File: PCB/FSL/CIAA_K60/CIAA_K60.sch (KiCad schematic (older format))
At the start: 12 parts

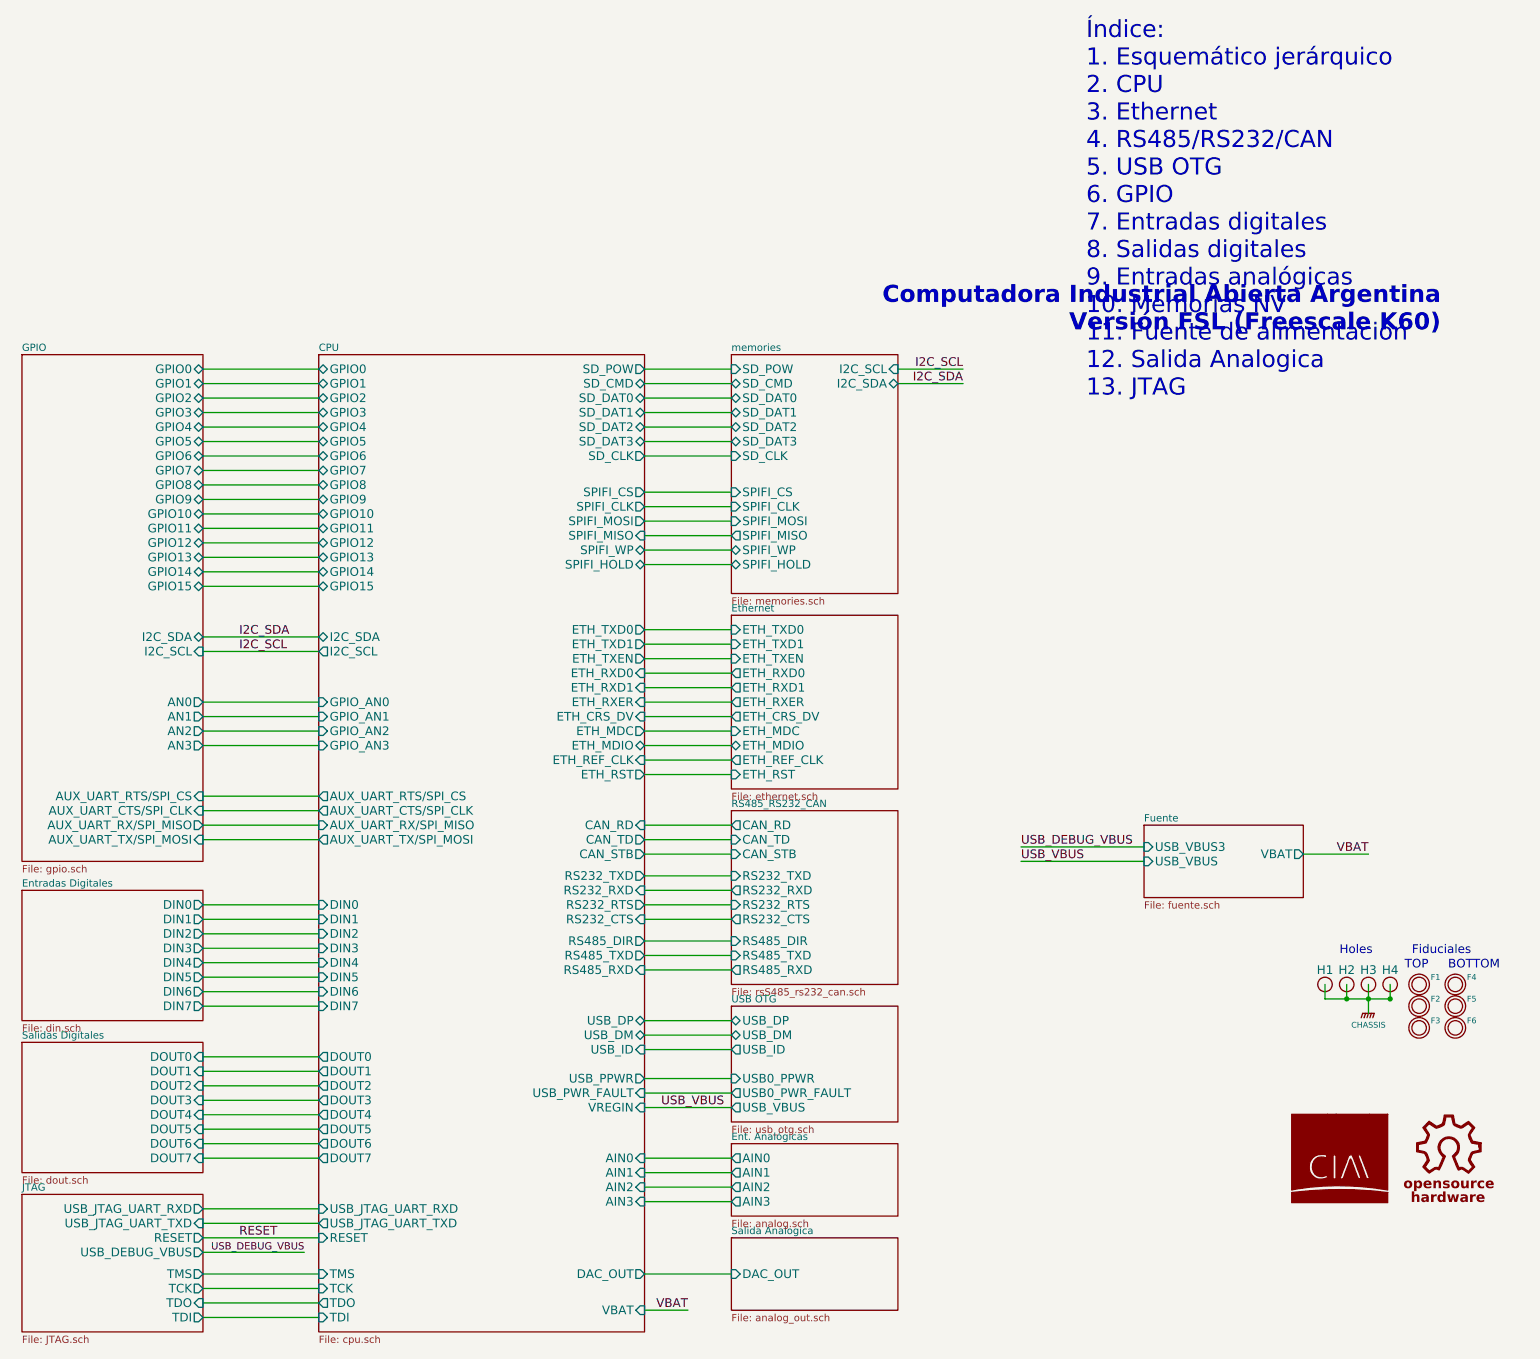
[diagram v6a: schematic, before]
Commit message: Sch files adapted to new eeschema. Fixing some text locations.
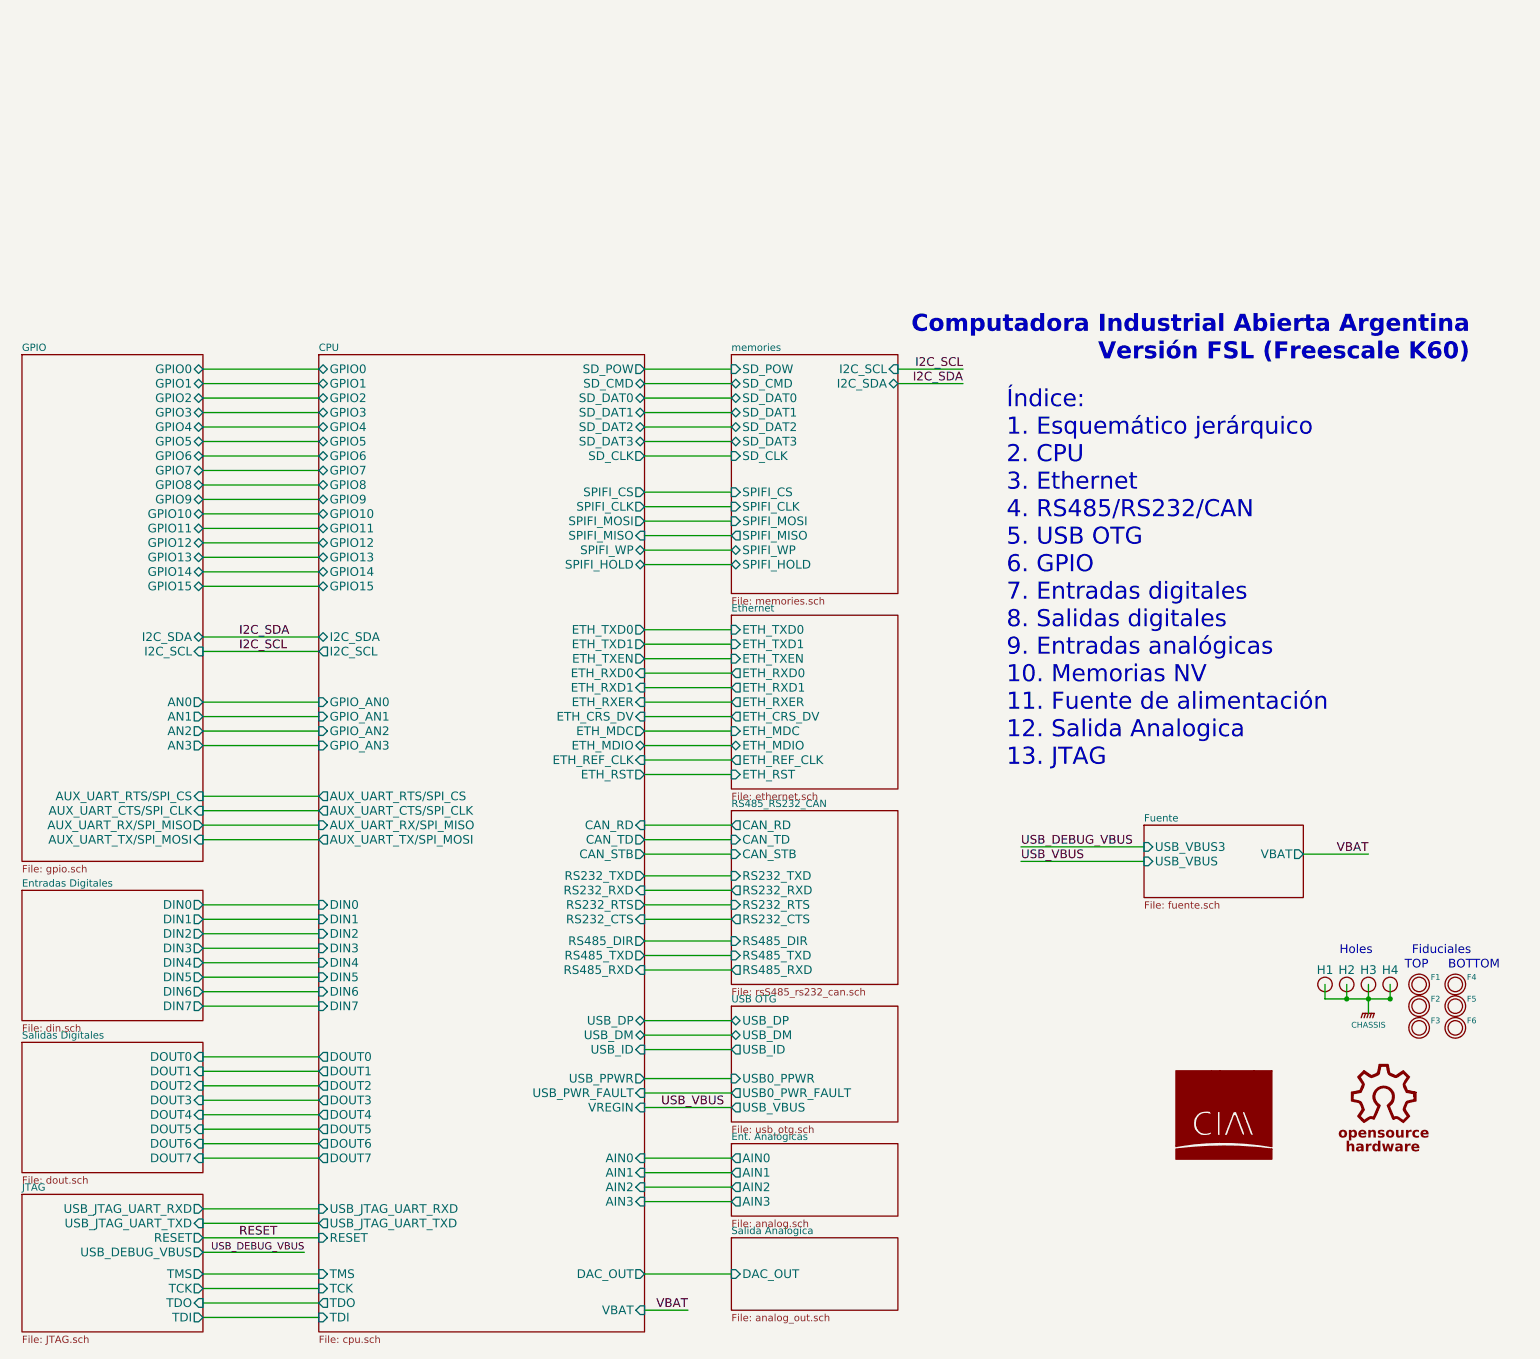
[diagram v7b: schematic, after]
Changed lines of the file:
@@
 EESchema Schematic File Version 2
 LIBS:CIAAK60LIB
-EELAYER 27 0
+LIBS:CIAA_K60-cache
+EELAYER 25 0
 EELAYER END
 $Descr A4 11693 8268
@@
 F9 "RESET" O R 2150 6950 60
 $EndSheet
-Text Notes 8250 1150 0    118  ~ 0
+Text Notes 7700 3700 0    118  ~ 0
 Índice:\n1. Esquemático jerárquico\n2. CPU\n3. Ethernet\n4. RS485/RS232/CAN\n5. USB OTG\n6. GPIO\n7. Entradas digitales\n8. Salidas digitales\n9. Entradas analógicas\n10. Memorias NV\n11. Fuente de alimentación\n12. Salida Analogica\n13. JTAG\n
-Text Notes 10700 700  2    118  ~ 24
+Text Notes 10900 900  2    118  ~ 24
 Computadora Industrial Abierta Argentina\nVersión FSL (Freescale K60)
 Text Label 7800 4250 0    60   ~ 0
@@
 L OSHWA G101
 U 1 1 53A0DEBC
-P 10750 6400
-F 0 "G101" H 10720 6800 60  0001 C CNN
-F 1 "OSHWA" H 10750 6703 60  0001 C CNN
-F 2 "OSHWA" H 10750 6400 60  0001 C CNN
-F 3 "~" H 10750 6400 60  0000 C CNN
-F 4 "LOGO DE OPEN SOURCE HARDWARE" H 10750 6400 60  0001 C CNN "Descripcion"
-	1    10750 6400
+P 10300 6050
+F 0 "G101" H 10270 6450 60  0001 C CNN
+F 1 "OSHWA" H 10300 6353 60  0001 C CNN
+F 2 "OSHWA" H 10300 6050 60  0001 C CNN
+F 3 "~" H 10300 6050 60  0000 C CNN
+F 4 "LOGO DE OPEN SOURCE HARDWARE" H 10300 6050 60  0001 C CNN "Descripcion"
+	1    10300 6050
 	1    0    0    -1
 $EndComp
@@
 L LOGO_CIAA G102
 U 1 1 53E44CA2
-P 10000 6400
-F 0 "G102" H 10000 5827 60  0001 C CNN
-F 1 "LOGO_CIAA" H 10000 6973 60  0001 C CNN
-F 2 "LOGO-CIAA" H 10000 6400 60  0001 C CNN
-F 3 "~" H 10000 6400 60  0000 C CNN
-F 4 "LOGO CIAA" H 10000 6400 60  0001 C CNN "Descripcion"
-	1    10000 6400
-	1    0    0    -1
-$EndComp
+P 9200 6100
+F 0 "G102" H 9200 5527 60  0001 C CNN
+F 1 "LOGO_CIAA" H 9200 6673 60  0001 C CNN
+F 2 "LOGO-CIAA" H 9200 6100 60  0001 C CNN
+F 3 "~" H 9200 6100 60  0000 C CNN
+F 4 "LOGO CIAA" H 9200 6100 60  0001 C CNN "Descripcion"
+	1    9200 6100
+	1    0    0    -1
+$EndComp

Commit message: Renaming symbol field-names in .sch files for KiCost integration.
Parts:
- F1, F2, F3, F4, F5, F6: Desc (none) -> FIDUCIAL; Descripcion FIDUCIAL -> (none)
- G101: Desc (none) -> LOGO DE OPEN SOURCE HARDWARE; Descripcion LOGO DE OPEN SOURCE HARDWARE -> (none)
- G102: Desc (none) -> LOGO CIAA; Descripcion LOGO CIAA -> (none)
- H1, H2, H3, H4: Desc (none) -> PCB HOLE; Descripcion PCB HOLE -> (none)
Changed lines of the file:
@@
 F 2 "Fiducial_1mm" H 10550 5250 60  0001 C CNN
 F 3 "~" H 10550 5250 60  0001 C CNN
-F 4 "FIDUCIAL" H 10600 5000 60  0001 C CNN "Descripcion"
-F 5 "~" H 10830 5400 60  0001 C CNN "Fabricante"
-F 6 "~" H 10930 5500 60  0001 C CNN "Nro. parte"
+F 4 "FIDUCIAL" H 10600 5000 60  0001 C CNN "Desc"
+F 5 "~" H 10830 5400 60  0001 C CNN "Manf"
+F 6 "~" H 10930 5500 60  0001 C CNN "Manf#"
 F 7 "~" H 11030 5600 60  0001 C CNN "Path datasheet"
-F 8 "~" H 11130 5700 60  0001 C CNN "Digikey/Mouser"
+F 8 "~" H 11130 5700 60  0001 C CNN "Digikey#"
 F 9 "~" H 11230 5800 60  0001 C CNN "Footprint estandar"
 	1    10550 5200
@@
 F 2 "PCB_HOLE" H 9750 5250 60  0001 C CNN
 F 3 "~" H 9850 5350 60  0001 C CNN
-F 4 "PCB HOLE" H 9950 5450 60  0001 C CNN "Descripcion"
-F 5 "~" H 10050 5550 60  0001 C CNN "Fabricante"
-F 6 "~" H 10150 5650 60  0001 C CNN "Nro. parte"
+F 4 "PCB HOLE" H 9950 5450 60  0001 C CNN "Desc"
+F 5 "~" H 10050 5550 60  0001 C CNN "Manf"
+F 6 "~" H 10150 5650 60  0001 C CNN "Manf#"
 F 7 "~" H 10250 5750 60  0001 C CNN "Path datasheet"
-F 8 "~" H 10350 5850 60  0001 C CNN "Digikey/Mouser"
+F 8 "~" H 10350 5850 60  0001 C CNN "Digikey#"
 F 9 "~" H 10450 5950 60  0001 C CNN "Footprint estandar"
 	1    9900 5200
@@
 F 2 "Fiducial_1mm" H 10550 5400 60  0001 C CNN
 F 3 "~" H 10550 5400 60  0001 C CNN
-F 4 "FIDUCIAL" H 10600 5150 60  0001 C CNN "Descripcion"
-F 5 "~" H 10830 5550 60  0001 C CNN "Fabricante"
-F 6 "~" H 10930 5650 60  0001 C CNN "Nro. parte"
+F 4 "FIDUCIAL" H 10600 5150 60  0001 C CNN "Desc"
+F 5 "~" H 10830 5550 60  0001 C CNN "Manf"
+F 6 "~" H 10930 5650 60  0001 C CNN "Manf#"
 F 7 "~" H 11030 5750 60  0001 C CNN "Path datasheet"
-F 8 "~" H 11130 5850 60  0001 C CNN "Digikey/Mouser"
+F 8 "~" H 11130 5850 60  0001 C CNN "Digikey#"
 F 9 "~" H 11230 5950 60  0001 C CNN "Footprint estandar"
 	1    10550 5350
@@
 F 2 "Fiducial_1mm" H 10550 5550 60  0001 C CNN
 F 3 "~" H 10550 5550 60  0001 C CNN
-F 4 "FIDUCIAL" H 10600 5300 60  0001 C CNN "Descripcion"
-F 5 "~" H 10830 5700 60  0001 C CNN "Fabricante"
-F 6 "~" H 10930 5800 60  0001 C CNN "Nro. parte"
+F 4 "FIDUCIAL" H 10600 5300 60  0001 C CNN "Desc"
+F 5 "~" H 10830 5700 60  0001 C CNN "Manf"
+F 6 "~" H 10930 5800 60  0001 C CNN "Manf#"
 F 7 "~" H 11030 5900 60  0001 C CNN "Path datasheet"
-F 8 "~" H 11130 6000 60  0001 C CNN "Digikey/Mouser"
+F 8 "~" H 11130 6000 60  0001 C CNN "Digikey#"
 F 9 "~" H 11230 6100 60  0001 C CNN "Footprint estandar"
 	1    10550 5500
@@
 F 2 "Fiducial_1mm" H 10800 5250 60  0001 C CNN
 F 3 "~" H 10800 5250 60  0001 C CNN
-F 4 "FIDUCIAL" H 10850 5000 60  0001 C CNN "Descripcion"
-F 5 "~" H 11080 5400 60  0001 C CNN "Fabricante"
-F 6 "~" H 11180 5500 60  0001 C CNN "Nro. parte"
+F 4 "FIDUCIAL" H 10850 5000 60  0001 C CNN "Desc"
+F 5 "~" H 11080 5400 60  0001 C CNN "Manf"
+F 6 "~" H 11180 5500 60  0001 C CNN "Manf#"
 F 7 "~" H 11280 5600 60  0001 C CNN "Path datasheet"
-F 8 "~" H 11380 5700 60  0001 C CNN "Digikey/Mouser"
+F 8 "~" H 11380 5700 60  0001 C CNN "Digikey#"
 F 9 "~" H 11480 5800 60  0001 C CNN "Footprint estandar"
 	1    10800 5200
@@
 F 2 "Fiducial_1mm" H 10800 5400 60  0001 C CNN
 F 3 "~" H 10800 5400 60  0001 C CNN
-F 4 "FIDUCIAL" H 10850 5150 60  0001 C CNN "Descripcion"
-F 5 "~" H 11080 5550 60  0001 C CNN "Fabricante"
-F 6 "~" H 11180 5650 60  0001 C CNN "Nro. parte"
+F 4 "FIDUCIAL" H 10850 5150 60  0001 C CNN "Desc"
+F 5 "~" H 11080 5550 60  0001 C CNN "Manf"
+F 6 "~" H 11180 5650 60  0001 C CNN "Manf#"
 F 7 "~" H 11280 5750 60  0001 C CNN "Path datasheet"
-F 8 "~" H 11380 5850 60  0001 C CNN "Digikey/Mouser"
+F 8 "~" H 11380 5850 60  0001 C CNN "Digikey#"
 F 9 "~" H 11480 5950 60  0001 C CNN "Footprint estandar"
 	1    10800 5350
@@
 F 2 "Fiducial_1mm" H 10800 5550 60  0001 C CNN
 F 3 "~" H 10800 5550 60  0001 C CNN
-F 4 "FIDUCIAL" H 10850 5300 60  0001 C CNN "Descripcion"
-F 5 "~" H 11080 5700 60  0001 C CNN "Fabricante"
-F 6 "~" H 11180 5800 60  0001 C CNN "Nro. parte"
+F 4 "FIDUCIAL" H 10850 5300 60  0001 C CNN "Desc"
+F 5 "~" H 11080 5700 60  0001 C CNN "Manf"
+F 6 "~" H 11180 5800 60  0001 C CNN "Manf#"
 F 7 "~" H 11280 5900 60  0001 C CNN "Path datasheet"
-F 8 "~" H 11380 6000 60  0001 C CNN "Digikey/Mouser"
+F 8 "~" H 11380 6000 60  0001 C CNN "Digikey#"
 F 9 "~" H 11480 6100 60  0001 C CNN "Footprint estandar"
 	1    10800 5500
@@
 F 2 "PCB_HOLE" H 9900 5250 60  0001 C CNN
 F 3 "~" H 10000 5350 60  0001 C CNN
-F 4 "PCB HOLE" H 10100 5450 60  0001 C CNN "Descripcion"
-F 5 "~" H 10200 5550 60  0001 C CNN "Fabricante"
-F 6 "~" H 10300 5650 60  0001 C CNN "Nro. parte"
+F 4 "PCB HOLE" H 10100 5450 60  0001 C CNN "Desc"
+F 5 "~" H 10200 5550 60  0001 C CNN "Manf"
+F 6 "~" H 10300 5650 60  0001 C CNN "Manf#"
 F 7 "~" H 10400 5750 60  0001 C CNN "Path datasheet"
-F 8 "~" H 10500 5850 60  0001 C CNN "Digikey/Mouser"
+F 8 "~" H 10500 5850 60  0001 C CNN "Digikey#"
 F 9 "~" H 10600 5950 60  0001 C CNN "Footprint estandar"
 	1    10050 5200
@@
 F 2 "PCB_HOLE" H 10050 5250 60  0001 C CNN
 F 3 "~" H 10150 5350 60  0001 C CNN
-F 4 "PCB HOLE" H 10250 5450 60  0001 C CNN "Descripcion"
-F 5 "~" H 10350 5550 60  0001 C CNN "Fabricante"
-F 6 "~" H 10450 5650 60  0001 C CNN "Nro. parte"
+F 4 "PCB HOLE" H 10250 5450 60  0001 C CNN "Desc"
+F 5 "~" H 10350 5550 60  0001 C CNN "Manf"
+F 6 "~" H 10450 5650 60  0001 C CNN "Manf#"
 F 7 "~" H 10550 5750 60  0001 C CNN "Path datasheet"
-F 8 "~" H 10650 5850 60  0001 C CNN "Digikey/Mouser"
+F 8 "~" H 10650 5850 60  0001 C CNN "Digikey#"
 F 9 "~" H 10750 5950 60  0001 C CNN "Footprint estandar"
 	1    10200 5200
@@
 F 2 "PCB_HOLE" H 10200 5250 60  0001 C CNN
 F 3 "~" H 10300 5350 60  0001 C CNN
-F 4 "PCB HOLE" H 10400 5450 60  0001 C CNN "Descripcion"
-F 5 "~" H 10500 5550 60  0001 C CNN "Fabricante"
-F 6 "~" H 10600 5650 60  0001 C CNN "Nro. parte"
+F 4 "PCB HOLE" H 10400 5450 60  0001 C CNN "Desc"
+F 5 "~" H 10500 5550 60  0001 C CNN "Manf"
+F 6 "~" H 10600 5650 60  0001 C CNN "Manf#"
 F 7 "~" H 10700 5750 60  0001 C CNN "Path datasheet"
-F 8 "~" H 10800 5850 60  0001 C CNN "Digikey/Mouser"
+F 8 "~" H 10800 5850 60  0001 C CNN "Digikey#"
 F 9 "~" H 10900 5950 60  0001 C CNN "Footprint estandar"
 	1    10350 5200
@@
 F 2 "OSHWA" H 10300 6050 60  0001 C CNN
 F 3 "~" H 10300 6050 60  0000 C CNN
-F 4 "LOGO DE OPEN SOURCE HARDWARE" H 10300 6050 60  0001 C CNN "Descripcion"
+F 4 "LOGO DE OPEN SOURCE HARDWARE" H 10300 6050 60  0001 C CNN "Desc"
 	1    10300 6050
 	1    0    0    -1
@@
 F 2 "LOGO-CIAA" H 9200 6100 60  0001 C CNN
 F 3 "~" H 9200 6100 60  0000 C CNN
-F 4 "LOGO CIAA" H 9200 6100 60  0001 C CNN "Descripcion"
+F 4 "LOGO CIAA" H 9200 6100 60  0001 C CNN "Desc"
 	1    9200 6100
 	1    0    0    -1
